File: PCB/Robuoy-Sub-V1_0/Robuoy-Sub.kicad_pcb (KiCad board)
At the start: 4 copper layers, 114 parts, among them J101 PROG/JTAG, J102 TO PUSH BUTTON, J103 ESC_BB, J104 ESC_SB, J105 RS232_Option, J106 Compass, J201 Accu, J202 LoadbalanceAccu1, J203 LoadbalanceAccu2, J204 Conn_01x10, J205 PWR_Charger, J206 LoadbalanceCharger, J207 ESCSB, J208 ESCBB, Q101 AO3400A, Q201 AO3400A, Q202 AO3400A, Q203 AO3400A, Q204 AO3400A, Q205 AO3400A, Q206 AO3400A, Q207 AO3400A, Q208 AO3400A, SW101 ~{BOOT}, SW102 ~{RESET}, SW201 SS-12D11-G050/On-Off, U101 ESP32-WROOM-32E_(visible_peri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, U102 USBLC6-4SC6, U103 LTC4311, U104 SN74LV1T34DBV, U105 SN74LV1T34DBV, U201 TPS5430DDAR, U202 SN74LV1T34DBV, U203 SN74LV1T34DBV, U204 TLV61046ADB

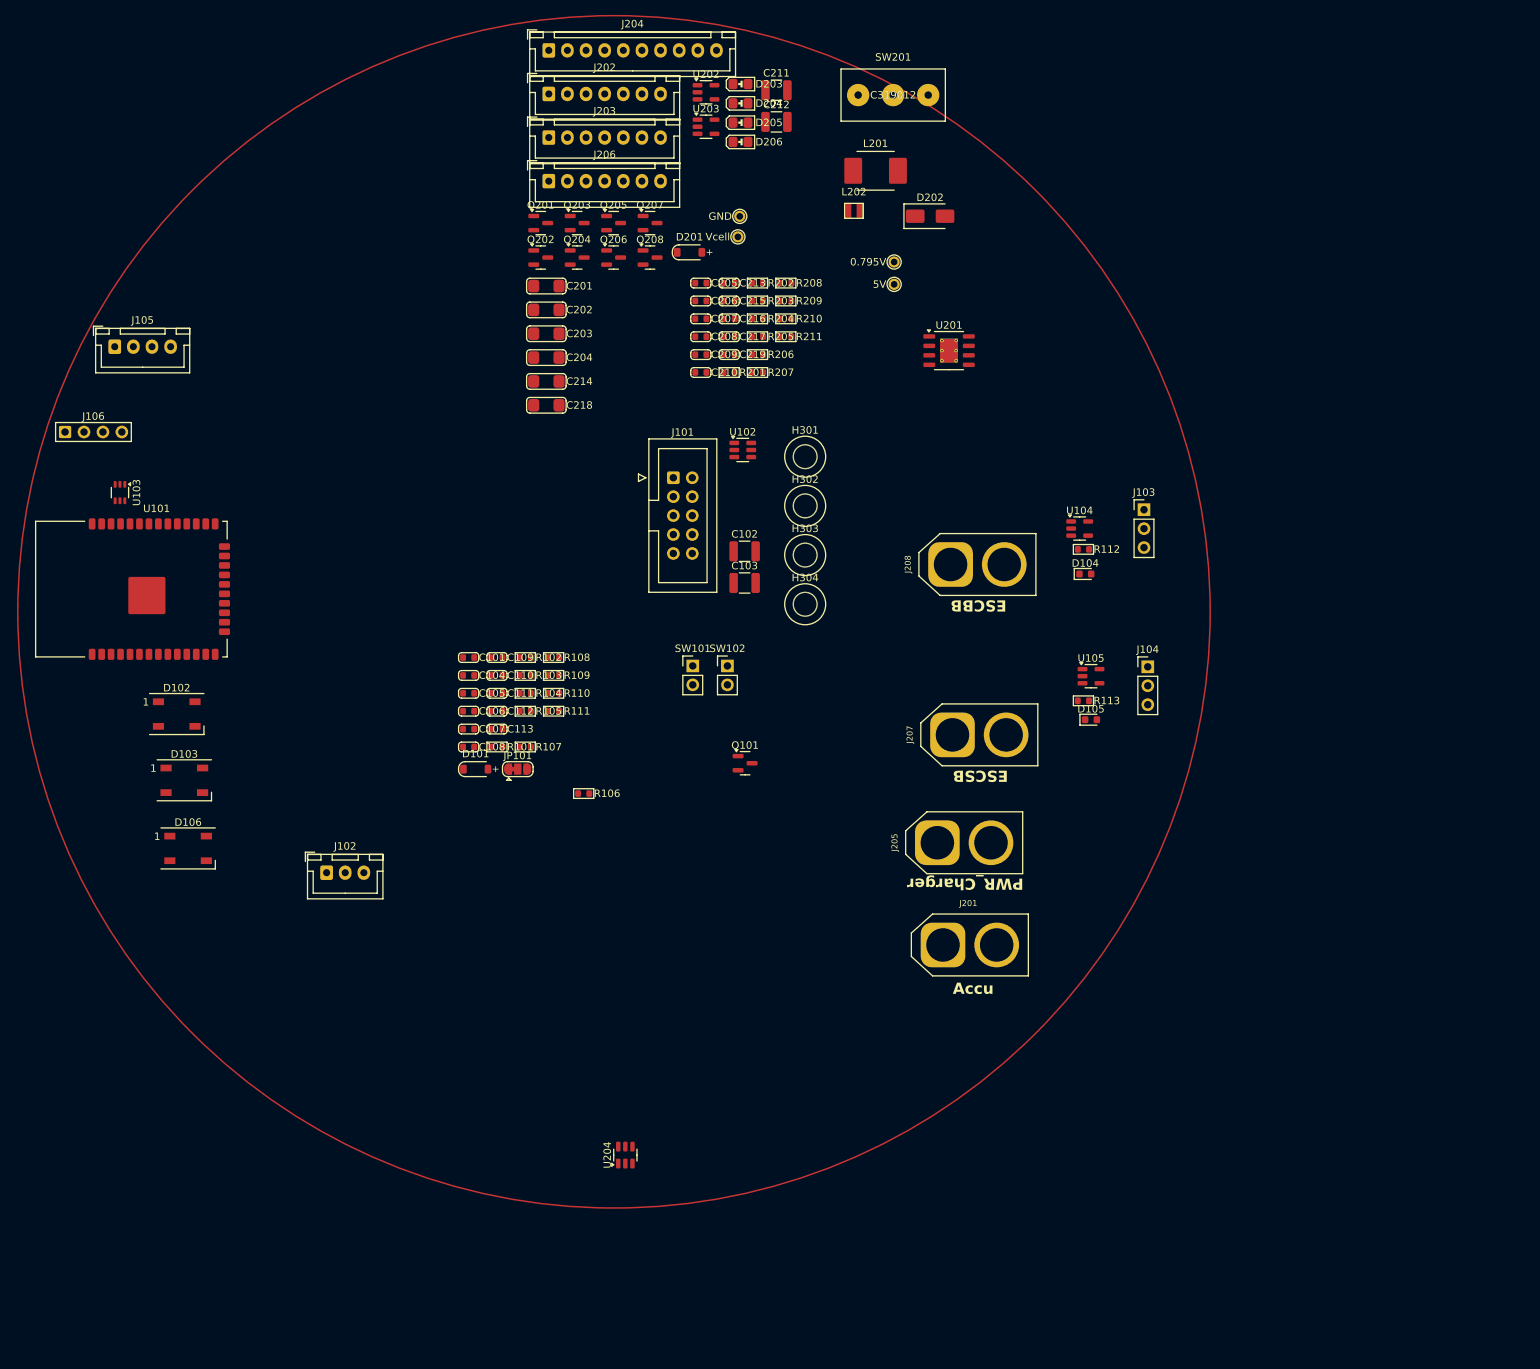
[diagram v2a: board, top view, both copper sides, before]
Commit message: PCB changes. Calulation price changed
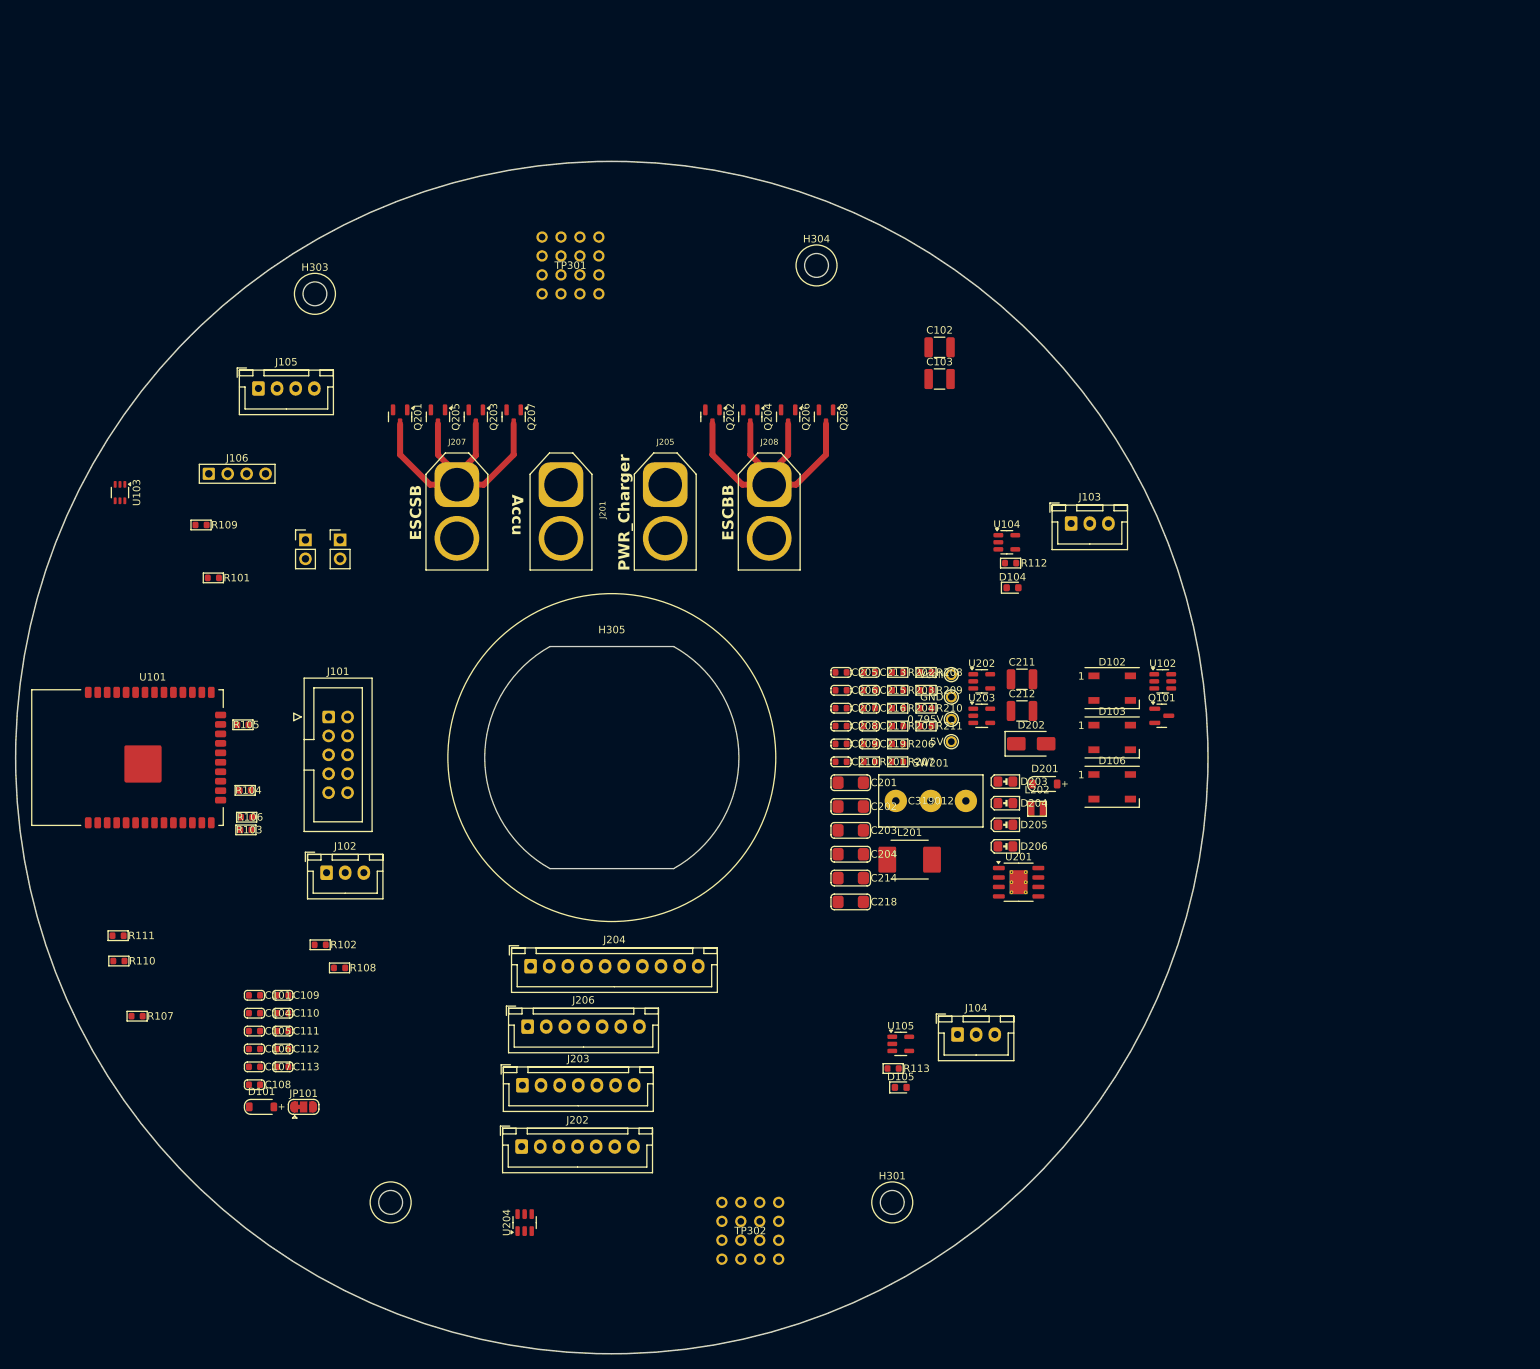
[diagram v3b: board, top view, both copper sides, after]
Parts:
- added H305: GX16_CutOut, A_Mechanical:GX16_CutOut, F.Cu at (94.5, 115.4)
- added TP301: RW1, A_Misc:ReworkPins, F.Cu at (89.0, 49.4)
- added TP302: RW2, A_Misc:ReworkPins, F.Cu at (113.1, 178.9)
- J103, J104: footprint Connector_PinHeader_2.54mm:PinHeader_1x03_P2.54mm_Vertical -> Connector_JST:JST_XH_B3B-XH-A_1x03_P2.50mm_Vertical
- moved J202 141.3 mm to (82.4, 167.6)
- moved J203 127.2 mm to (82.5, 159.4)
- moved D102 125.6 mm to (161.7, 106.1)
- moved D103 124.6 mm to (161.7, 112.7)
- moved D106 124.3 mm to (161.7, 119.3)
- moved J204 122.9 mm to (83.6, 143.4)
- moved J206 113.5 mm to (83.2, 151.5)
- moved H302 108.8 mm to (64.8, 175.1)
- moved D206 101.0 mm to (147.3, 127.3)
- moved H301 100.7 mm to (132.1, 175.1)
- moved D205 100.7 mm to (147.3, 124.4)
- moved D204 100.4 mm to (147.3, 121.5)
- moved D203 100.1 mm to (147.3, 118.6)
- moved SW201 94.9 mm to (137.3, 121.2)
- moved L201 92.5 mm to (134.5, 129.1)
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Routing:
- net Net-(D205-K): track 0.00 -> 45.3 mm
- net Net-(D206-K): track 0.00 -> 43.8 mm
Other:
- board outline added: 160 x 160 mm

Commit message: Sub PCB parts okay
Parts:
- removed H305: GX16_CutOut, A_Mechanical:GX16_CutOut
- added BZ101: Buzzer, A_Misc:Buzzer-12x6.5x5.2, F.Cu at (70.3, 46.6)
- added Q102: AO3400A, Package_TO_SOT_SMD:SOT-23, F.Cu at (65.8, 56.0)
- added R114: 100, A_Device:R_0603, F.Cu at (79.3, 40.8)
- added R115: 100, A_Device:R_0603, F.Cu at (79.3, 43.2)
- added R116: 100, A_Device:R_0603, F.Cu at (79.3, 45.6)
- added TP101: BUZZER, A_Pads_Pins:Testpad_2, F.Cu at (100.4, 39.2)
- added TP102: ESC_BB, A_Pads_Pins:Testpad_2, F.Cu at (100.4, 41.7)
- added TP103: ESC_SB, A_Pads_Pins:Testpad_2, F.Cu at (105.5, 62.0)
- added TP104: LEDS, A_Pads_Pins:Testpad_2, F.Cu at (135.9, 79.8)
- added TP105: ESC_BB-5V, A_Pads_Pins:Testpad_2, F.Cu at (95.3, 59.5)
- added TP106: ESC_SB-5V, A_Pads_Pins:Testpad_2, F.Cu at (115.6, 39.2)
- added TP107: SDA, A_Pads_Pins:Testpad_2, F.Cu at (105.9, 48.0)
- added TP108: SCL, A_Pads_Pins:Testpad_2, F.Cu at (105.9, 51.0)
- added TP109: RXD, A_Pads_Pins:Testpad_2, F.Cu at (105.9, 54.0)
- added TP110: TXD, A_Pads_Pins:Testpad_2, F.Cu at (105.5, 57.0)
- added TP205: 5V, A_Pads_Pins:Testpad_2, F.Cu at (62.3, 87.5)
- added TP206: 1.221V, A_Pads_Pins:Testpad_2, F.Cu at (115.6, 41.7)
- added TP207: ESC_BB-POWER, A_Pads_Pins:Testpad_2, F.Cu at (115.6, 44.3)
- added TP208: ESC_SB-POWER, A_Pads_Pins:Testpad_2, F.Cu at (128.3, 59.5)
- added TP209: ESC_BB-POWER-5V, A_Pads_Pins:Testpad_2, F.Cu at (128.3, 57.0)
- added TP210: ESC_SB-POWER-5V, A_Pads_Pins:Testpad_2, F.Cu at (128.3, 62.0)
- J102: value TO PUSH BUTTON -> PUSH BUTTON
- J105: footprint Connector_JST:JST_XH_B4B-XH-A_1x04_P2.50mm_Vertical -> Connector_PinSocket_2.54mm:PinSocket_1x04_P2.54mm_Vertical
- J106: footprint A_Connector:Header_1x04_P2.54_Male -> Connector_JST:JST_XH_B4B-XH-A_1x04_P2.50mm_Vertical
- J204: value Conn_01x10 -> CHARGE/ON-OFF; footprint Connector_JST:JST_XH_B10B-XH-A_1x10_P2.50mm_Vertical -> A_Connector:T4140012121000
- TP201: footprint A_Pads_Pins:Testpoint_0.9x1.5 -> A_Pads_Pins:Testpad_2
- TP202: footprint A_Pads_Pins:Testpoint_0.9x1.5 -> TestPoint:TestPoint_Loop_D2.54mm_Drill1.5mm_Beaded
- TP203: value 0.795V -> GND; footprint A_Pads_Pins:Testpoint_0.9x1.5 -> TestPoint:TestPoint_Loop_D2.54mm_Drill1.5mm_Beaded
- TP204: value 5V -> 0.795V; footprint A_Pads_Pins:Testpoint_0.9x1.5 -> A_Pads_Pins:Testpad_2
- moved TP203 54.9 mm to (90.7, 134.4)
- moved TP202 42.1 mm to (107.5, 133.9)
- moved J204 36.8 mm to (92.8, 107.8)
- moved SW101 27.9 mm to (67.4, 110.3), turned to -90 degrees
- moved SW102 21.2 mm to (67.4, 105.2), turned to -90 degrees
- moved R106 8.15 mm to (47.0, 115.4)
- moved R103 7.35 mm to (47.0, 117.9)
- moved R104 7.15 mm to (47.0, 112.8)
- moved J105 6.85 mm to (44.5, 59.5)
- moved R105 6.11 mm to (47.0, 105.2)
- moved U101 5.41 mm to (30.0, 110.0)
- moved J101 5.18 mm to (55.0, 105.0)
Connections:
- J103 pad 3: GND -> Net-(J103-Pin_3)
- J104 pad 3: GND -> Net-(J104-Pin_3)
- J204 pad 10: Vbatt -> GND
- TP203 pad 1: Net-(U204-FB) -> GND
- TP204 pad 1: +5V -> Net-(U204-FB)
- U101 pad 26: unconnected-(U101-D1/GPIO4-Pad26) -> BUZZER

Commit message: Top Pcb finished Botom Cup finished
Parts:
- added C114: 100n, A_Device:C_0603, F.Cu at (156.3, 71.1)
- added C115: 100u/16V, Capacitor_SMD:C_1210_3225Metric, F.Cu at (152.4, 67.8)
- added C116: 100n, A_Device:C_0603, F.Cu at (156.3, 73.5)
- added FB101: 0.3E 240E@100MHz, A_Device:L_0805_(1.2), F.Cu at (152.0, 71.3)
- added U106: LSM303AGRTR, Package_LGA:LGA-12_2x2mm_P0.5mm, F.Cu at (157.3, 67.7)

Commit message: PCB changed
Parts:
- SW201: value SS-12D11-G050/On-Off -> On/Off
- moved SW201 39.3 mm to (98.3, 126.2)
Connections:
- SW201 pad 3: (no net) -> unconnected-(SW201-Pad3)
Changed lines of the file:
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@@
 	(net 94 "unconnected-(U106-INT_MAG-Pad7)")
 	(net 95 "unconnected-(U106-INT_XL-Pad12)")
+	(net 96 "unconnected-(SW201-Pad3)")
 	(footprint "A_Passive:LED_0805"
 		(layer "F.Cu")
@@
 	(footprint "A_Connector:SS-12D10L5"
 		(layer "F.Cu")
-		(at 137.32 121.21)
+		(at 98.31 126.19)
 		(descr "Switch")
 		(property "Reference" "SW201"
@@
 			)
 		)
-		(property "Value" "SS-12D11-G050/On-Off"
-			(at 0 1 0)
+		(property "Value" "On/Off"
+			(at -0.5 4.7 0)
 			(unlocked yes)
-			(layer "F.Fab")
+			(layer "F.SilkS")
 			(effects
 				(font
@@
 			)
 		)
-		(property "Datasheet" "https://wmsc.lcsc.com/wmsc/upload/file/pdf/v2/lcsc/2110151630_XKB-Connection-SS-12D10L5_C319012.pdf"
+		(property "Datasheet" ""
 			(at 0 0 0)
 			(unlocked yes)
@@
 			)
 		)
-		(property "Description" "Single Pole Single Throw (SPST) switch, separate symbol"
+		(property "Description" ""
 			(at 0 0 0)
 			(unlocked yes)
@@
 			(at 0 0 0)
 			(unlocked yes)
-			(layer "F.SilkS")
+			(layer "F.Fab")
+			(hide yes)
 			(effects
 				(font
@@
 			)
 		)
-		(sheetname "PSU")
-		(sheetfile "PSU_sch.kicad_sch")
 		(attr through_hole)
 		(fp_line
@@
 		)
 		(fp_text user "${REFERENCE}"
-			(at 0 2.5 0)
+			(at -10.2 -0.1 0)
 			(unlocked yes)
-			(layer "F.Fab")
+			(layer "F.SilkS")
 			(effects
 				(font
@@
 			(remove_unused_layers no)
 			(net 9 "Vbatt")
-			(pinfunction "A")
 			(pintype "passive")
 		)
@@
 			(remove_unused_layers no)
 			(net 8 "+VSW")
-			(pinfunction "B")
 			(pintype "passive")
 		)
@@
 			(layers "*.Cu" "*.Mask")
 			(remove_unused_layers no)
+			(net 96 "unconnected-(SW201-Pad3)")
+			(pintype "passive")
 		)
 		(model "${USER_3D_MODEL}/Button_Switch/SS-12D10L4.STEP"

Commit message: Pcb edditing
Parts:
- removed J206: LoadbalanceCharger, Connector_JST:JST_XH_B7B-XH-A_1x07_P2.50mm_Vertical
- removed R103, R104, R105, R106: 100, A_Device:R_0603
- added D102: SM4007PL, A_Device:D_SOD-123_2.85x1.8x1.3, F.Cu at (169.3, 97.4)
- added H305: MountingHole, A_Mechanical:NPTH_M3, F.Cu at (70.8, 82.9)
- added H306: MountingHole, A_Mechanical:NPTH_M3, F.Cu at (70.8, 112.9)
- added H307: MountingHole, A_Mechanical:NPTH_M3, F.Cu at (180.8, 82.9)
- added H308: MountingHole, A_Mechanical:NPTH_M3, F.Cu at (180.8, 112.9)
- added R209: 100, A_Device:R_0603, F.Cu at (103.8, 124.4)
- added R211: 100, A_Device:R_0603, F.Cu at (141.8, 124.4)
- J201: value Accu -> Accu 1
- J205: value PWR_Charger -> Accu 2; footprint A_Connector:AMASS_XT60-F_1x02_P7.20mm_Vertical -> A_Connector:AMASS_XT60-M_1x02_P7.20mm_Vertical
- moved TP302 131.7 mm to (145.1, 51.1)
- moved R107 129.3 mm to (128.6, 65.4)
- moved R110 121.4 mm to (122.7, 66.3)
- moved R111 121.4 mm to (122.6, 62.9)
- moved C112 120.3 mm to (127.8, 62.4)
- moved C110 117.2 mm to (163.3, 118.4)
- moved Q102 113.4 mm to (167.9, 105.4)
- moved R112 105.5 mm to (168.8, 101.4)
- moved BZ101 105.1 mm to (166.8, 88.4)
- moved C104 102.5 mm to (109.1, 68.4)
- moved C105 102.5 mm to (109.1, 70.8)
- moved C106 102.5 mm to (109.1, 73.2)
- moved C108 102.5 mm to (109.1, 78.0)
- moved C109 102.5 mm to (112.9, 66.0)
- moved C107 102.5 mm to (109.1, 75.6)
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- renumbered C115 to C113, C116 to C114, C113 to C115, C114 to C116, D102 to D103, D103 to D104, D104 to D105, D105 to D106, D106 to D107, J105 to J103, J103 to J104, J104 to J105, R116 to R112, R112 to R113, R113 to R114, R114 to R115, R115 to R116, R209 to R210, R210 to R212, R211 to R213, TP109 to TP102, TP110 to TP103, TP108 to TP104, TP107 to TP105, TP104 to TP106, TP102 to TP107, TP103 to TP108, TP105 to TP109, TP106 to TP110, TP206 to TP202, TP208 to TP203, TP207 to TP204, TP202 to TP205, TP203 to TP206, TP210 to TP207, TP209 to TP208, TP204 to TP209, TP205 to TP210, U106 to U103, U103 to U104, U104 to U105, U105 to U106
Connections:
- J101 pad 10: Net-(J101-Pin_10) -> MTDI
- J101 pad 7: Net-(J101-Pin_7) -> MTMS
- J101 pad 8: Net-(J101-Pin_8) -> MTCK
- J101 pad 9: Net-(J101-Pin_9) -> MTDO
- J204 pad 1: Net-(J202-Pin_1) -> Vbatt
- J204 pad 10: GND -> Net-(J202-Pin_3)
- J204 pad 11: Vbatt -> Net-(J202-Pin_2)
- J204 pad 12: Vbatt -> Net-(J202-Pin_1)
- J204 pad 2: Net-(J202-Pin_2) -> Vbatt
- J204 pad 3: Net-(J202-Pin_3) -> GND
- J204 pad 4: Net-(J202-Pin_4) -> GND
- J204 pad 5: Net-(J202-Pin_5) -> +VSW
- J204 pad 6: Net-(J202-Pin_6) -> Net-(J202-Pin_7)
- J204 pad 7: Net-(J202-Pin_7) -> Net-(J202-Pin_6)
- J204 pad 8: +VSW -> Net-(J202-Pin_5)
- J204 pad 9: GND -> Net-(J202-Pin_4)
- U202 pad 4: Net-(Q201-G) -> Net-(U202-Y)
- U203 pad 4: Net-(Q202-G) -> Net-(U203-Y)
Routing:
- net Net-(D205-K): track 45.3 -> 0.00 mm
- net Net-(D206-K): track 43.8 -> 0.00 mm
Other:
- board size 160 x 160 mm -> 117 x 104.1 mm

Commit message: Some more PCB eddiring
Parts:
- TP101, TP102, TP103, TP104, TP105, TP106, TP107, TP108, TP109, TP110, TP201, TP202, TP203, TP204, TP207, TP208, TP209, TP210: footprint A_Pads_Pins:Testpad_2 -> A_Pads_Pins:Testpad_1
- moved C212 89.8 mm to (162.4, 97.7), turned to 90 degrees
- moved C211 88.2 mm to (165.9, 97.8), turned to 90 degrees
- moved TP210 84.8 mm to (174.8, 98.8)
- moved L201 84.4 mm to (162.1, 104.7), turned to 90 degrees
- moved L202 81.4 mm to (169.4, 106.3), turned to -90 degrees
- moved U204 78.0 mm to (172.5, 106.4)
- moved C201 75.9 mm to (152.0, 122.0), turned to 180 degrees
- moved C218 73.4 mm to (172.5, 101.4), turned to 90 degrees
- moved D202 70.7 mm to (154.8, 110.3), turned to 180 degrees
- moved C214 70.6 mm to (168.5, 101.4)
- moved C101 70.2 mm to (36.7, 133.2)
- moved R101 70.2 mm to (46.0, 133.2)
- moved R102 70.2 mm to (35.2, 133.2)
- moved SW101 70.2 mm to (43.3, 131.9)
- moved SW102 70.2 mm to (39.8, 131.9)
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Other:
- board text added: "OFF"
- board text added: "ON"
